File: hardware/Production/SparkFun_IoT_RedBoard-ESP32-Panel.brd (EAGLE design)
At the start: 172.2 x 137.9 mm, 850 parts, among them J1 5.5x2.1mm Barrel, J13 QWIIC_RIGHT_ANGLE, J15 MICRO-SD-PUSH-PUSH-EXT-PIN, J2 USB C, J21 USB C, J22 USB_SOLDER_PADS, J23 M10NO_SILK, J28 QWIIC_RIGHT_ANGLE, J29 MICRO-SD-PUSH-PUSH-EXT-PIN, J3 USB_SOLDER_PADS, J30 5.5x2.1mm Barrel, J37 USB C, J38 USB_SOLDER_PADS, J39 M10NO_SILK, J44 QWIIC_RIGHT_ANGLE, J45 MICRO-SD-PUSH-PUSH-EXT-PIN, J46 5.5x2.1mm Barrel, J5 M10NO_SILK, J53 USB C, J54 USB_SOLDER_PADS, J55 M10NO_SILK, J60 QWIIC_RIGHT_ANGLE, J61 MICRO-SD-PUSH-PUSH-EXT-PIN, J62 5.5x2.1mm Barrel, Q1 MBT3904DW1T1, Q11 20V/4.2A/52mΩ/1.4W, Q13 20V/4.2A/52mΩ/1.4W, Q14 MBT3904DW1T1, Q16 20V/4.2A/52mΩ/1.4W, Q18 20V/4.2A/52mΩ/1.4W, Q20 20V/4.2A/52mΩ/1.4W, Q22 20V/4.2A/52mΩ/1.4W, Q24 20V/4.2A/52mΩ/1.4W, Q26 20V/4.2A/52mΩ/1.4W, Q27 MBT3904DW1T1, Q29 20V/4.2A/52mΩ/1.4W, Q3 20V/4.2A/52mΩ/1.4W, Q31 20V/4.2A/52mΩ/1.4W, Q33 20V/4.2A/52mΩ/1.4W, Q35 20V/4.2A/52mΩ/1.4W, Q37 20V/4.2A/52mΩ/1.4W, Q39 20V/4.2A/52mΩ/1.4W, Q40 MBT3904DW1T1, Q42 20V/4.2A/52mΩ/1.4W, Q44 20V/4.2A/52mΩ/1.4W, Q46 20V/4.2A/52mΩ/1.4W, Q48 20V/4.2A/52mΩ/1.4W, Q5 20V/4.2A/52mΩ/1.4W, Q50 20V/4.2A/52mΩ/1.4W, Q52 20V/4.2A/52mΩ/1.4W, Q7 20V/4.2A/52mΩ/1.4W, Q9 20V/4.2A/52mΩ/1.4W, U1 ESP-WROOM-3232D-NARROW, U10 3.3V, U11 MCP73831, U12 MAX17048, U13 CH340C, U14 ESP-WROOM-3232D-NARROW, U15 LM1117, U16 3.3V, U17 MCP73831, U18 MAX17048, U19 CH340C, U2 CH340C, U20 ESP-WROOM-3232D-NARROW, U21 LM1117, U22 3.3V, U23 MCP73831, U24 MAX17048, U3 LM1117, U4 3.3V, U5 MCP73831, U6 MAX17048, U7 CH340C, U8 ESP-WROOM-3232D-NARROW, U9 LM1117

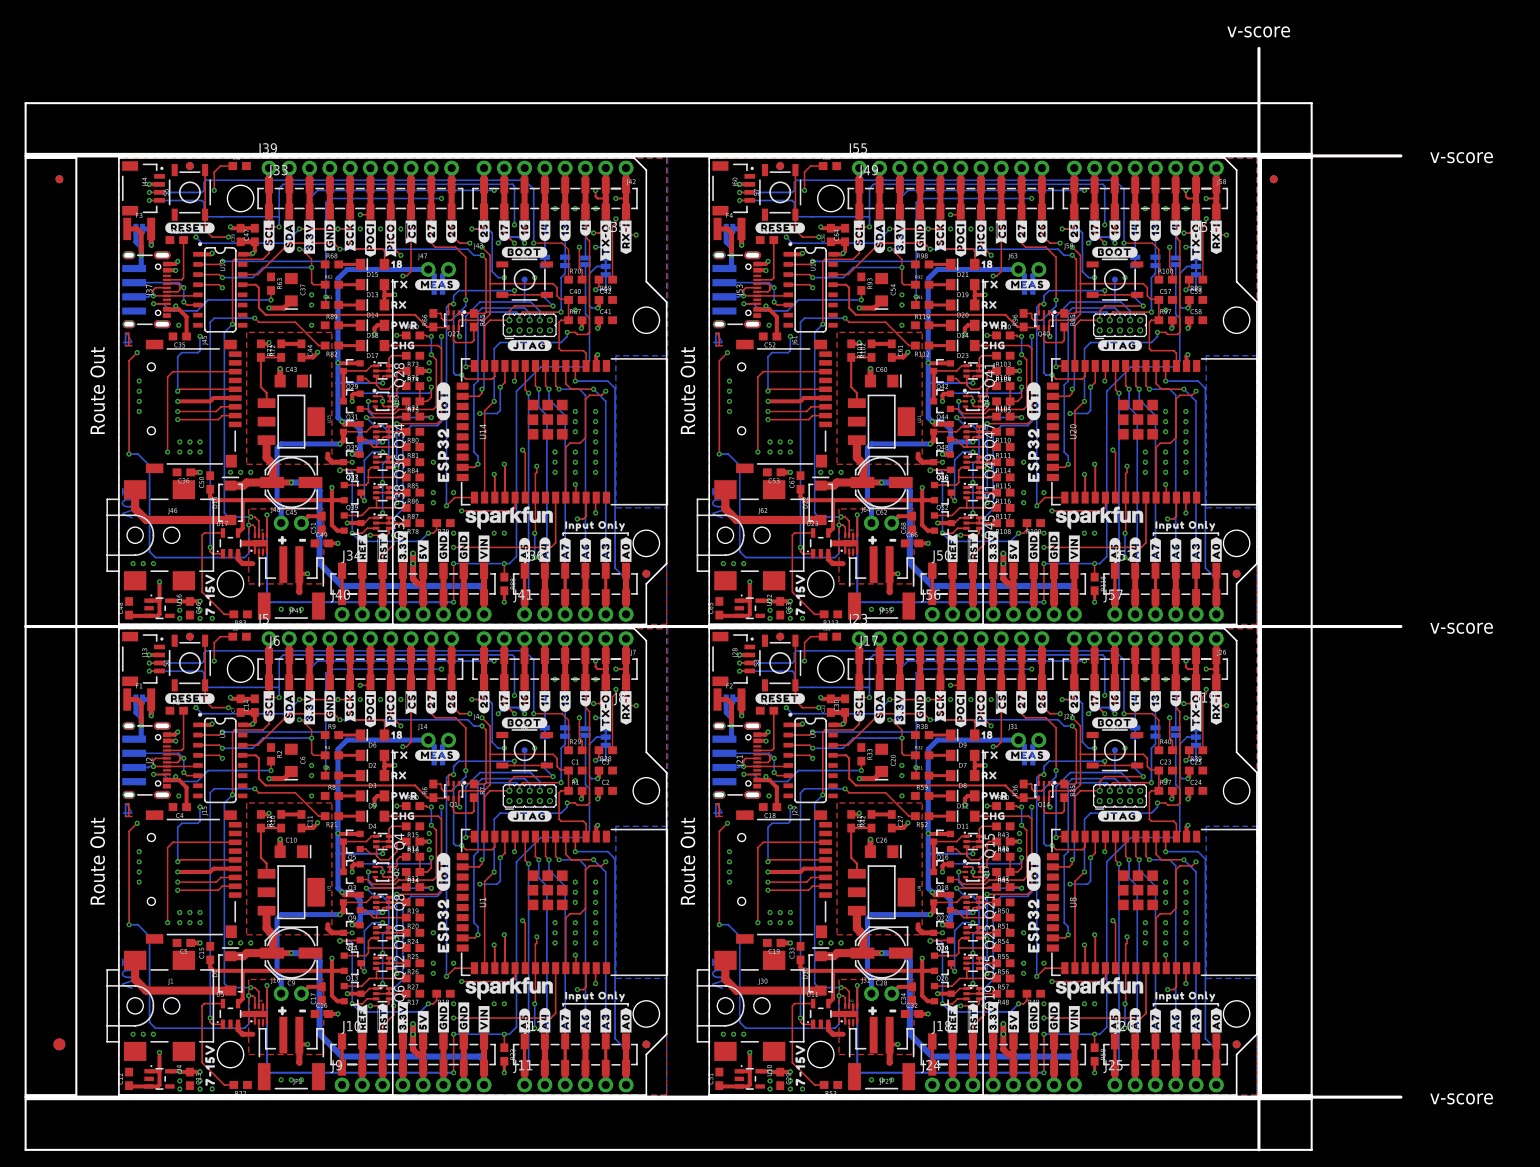
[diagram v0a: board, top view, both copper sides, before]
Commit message: Add production files for v02
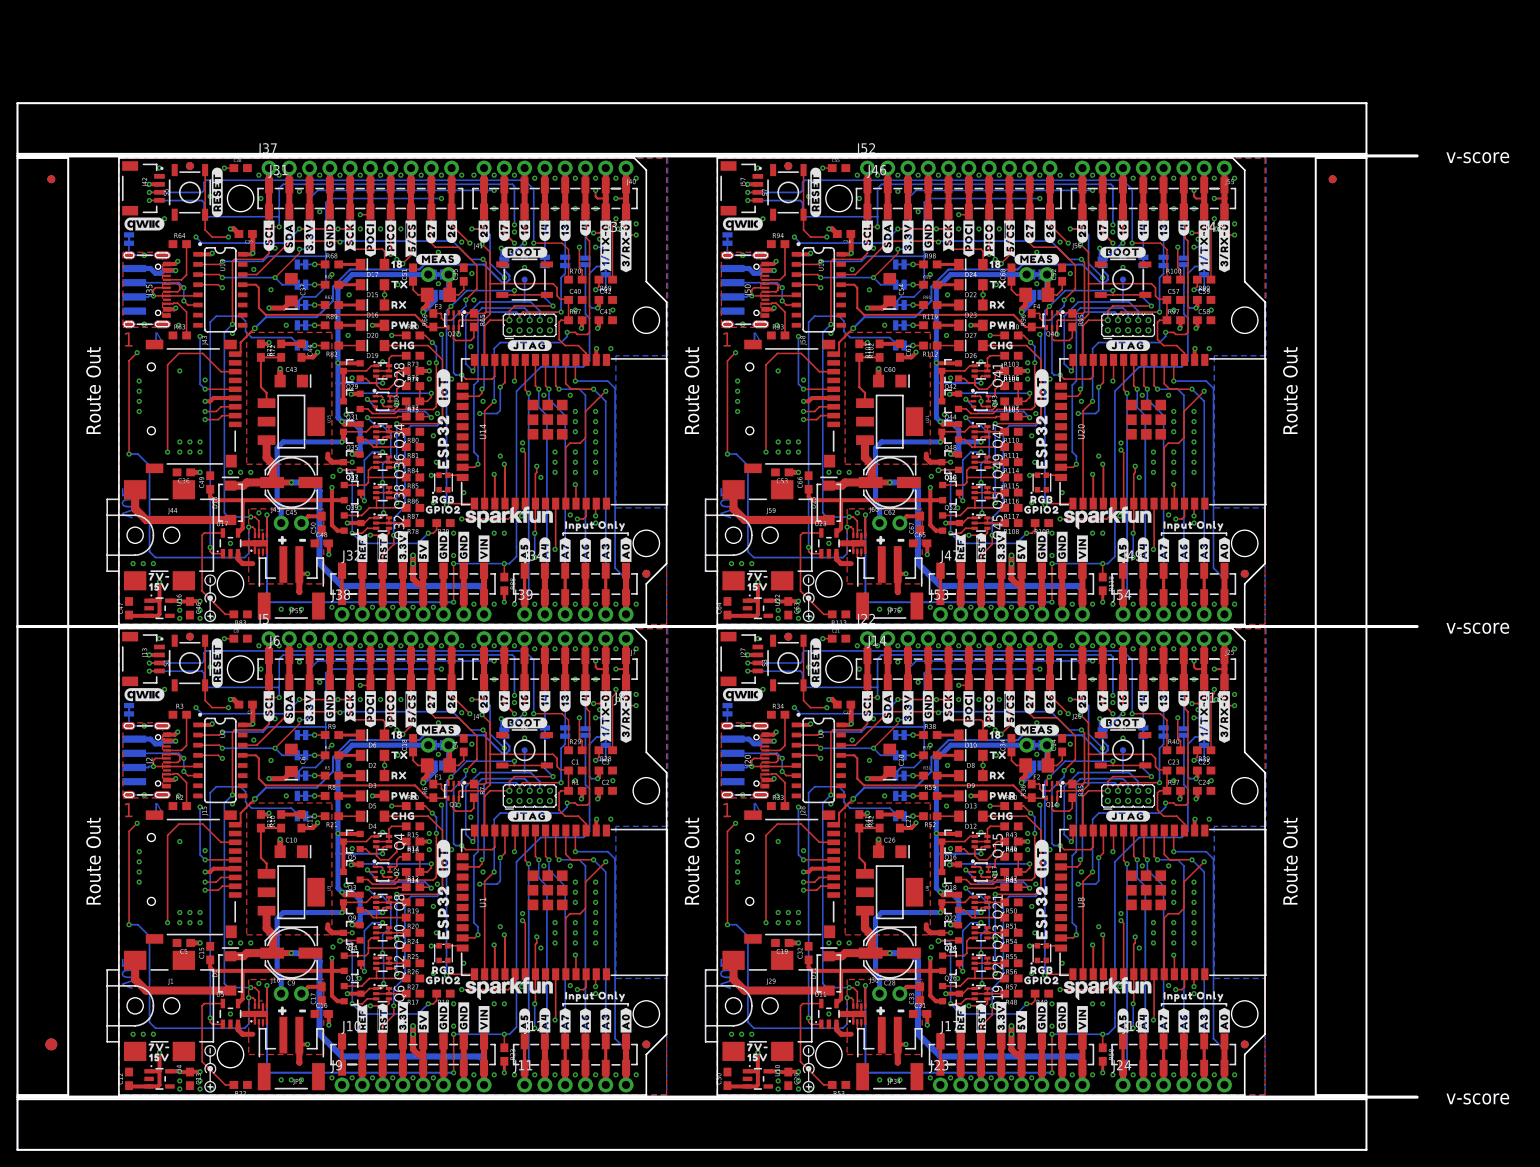
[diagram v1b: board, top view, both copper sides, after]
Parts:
- removed J61: MICRO-SD-PUSH-PUSH-EXT-PIN, SparkFun-Connectors:MICROSD-EXTERNALPIN
- removed J62: 5.5x2.1mm Barrel, SparkFun-Connectors:POWER_JACK_SMD
- removed J63, J64: (no value), SparkFun-Connectors:1X02_NO_SILK
- added D25: 3A/40V/500mV, SparkFun-DiscreteSemi:SMA-DIODE
- added D26: YELLOW, SparkFun-LED:LED-1206-HIDDENSILK
- added D27: GREEN, SparkFun-LED:LED-1206-HIDDENSILK
- added D28: WS2812_2020, SparkFun-LED:WS2812-2020
- added JP57, JP78: SHLD, SparkFun-Jumpers:SMT-JUMPER_2_NC_TRACE_SILK
- added JP58, JP79: SD_DET, SparkFun-Jumpers:SMT-JUMPER_2_NO_SILK
- added JP59, JP60, JP61, JP62, JP63, JP74, JP75, JP80, JP81, JP82, JP83, JP84: JUMPER-SMT_2_NC_TRACE_SILK, SparkFun-Jumpers:SMT-JUMPER_2_NC_TRACE_SILK
- added JP64, JP65, JP66, JP67: STAND-OFF, SparkFun-Hardware:STAND-OFF
- added JP68, JP69, JP70, JP71: FIDUCIAL1X2, SparkFun-Aesthetics:FIDUCIAL-1X2
- added JP72: JUMPER-SMT_3_2-NC_TRACE_SILK, SparkFun-Jumpers:SMT-JUMPER_3_2-NC_TRACE_SILK
- added JP73: JUMPER-SMT_2_NO_SILK, SparkFun-Jumpers:SMT-JUMPER_2_NO_SILK
- added JP76: LiPo, SparkFun-Connectors:JST-2-SMD
- added JP77: JUMPER-COMBO_2_NC_TRACE, SparkFun-Jumpers:COMBO-JUMPER_2_NC_TRACE
- added U$401: (no value), output-ESP32:G32321864
- added U$402: (no value), output-ESP32:#1849
- added U$403: (no value), output-ESP32:#1850
- added U$404: (no value), output-ESP32:#I2C#1855
- added U$405: (no value), output-ESP32:##ALERT##1852
- added U$406: (no value), output-ESP32:#TMS#1854
- added U$407: (no value), output-ESP32:#TCK#1853
- added U$408, U$409: (no value), output-ESP32:INPUT_ONLY321867
- added U$410: (no value), SparkFun-Aesthetics:REDBOARD_LOGO
- added U$411: (no value), output-ESP32:#IOT#132321869
- added U$412: (no value), output-ESP32:ESP32321856
- added U$413: (no value), output-ESP32:#IOT#132321874
- added U$414: (no value), output-ESP32:7#15V32321861
- added U$415: (no value), output-ESP32:3#3V_LOGIC_SHIELDS_ONLY132321876
- added U$416: (no value), output:#3#RX#0#0
- added U$417: (no value), output:#1#TX#0#0
- added U$418: (no value), output:#4##ALERT##0
- added U$419: (no value), output:#3#RX#0#4
- added U$420: (no value), output:#1#TX#0#2
- added U$421: (no value), output:#5##CS##0
- added U$422: (no value), output:#BYP#0
- added U$423: (no value), output:#SHLD#0
- added U$424: (no value), output:RGB0
- added U$425: (no value), output-ESP32:#MEAS#1851
- added U$426, U$427: (no value), SparkFun-Aesthetics:POLARITY_MARKING_CENTER_POSITIVE#JPG
- added U$428: (no value), output:7V#0
- added U$429: (no value), output:15V0
- added U$430: (no value), output:#SD_DET#0
- added U$431: (no value), output:#LED_18#0
- added U$432: (no value), output:#LED_TX#0
- added U$433: (no value), output:#LED_RX#0
- added U$434: (no value), output:#LED_PWR#0
- added U$435: (no value), output:#LED_CHG#0
- added U$436: (no value), output:GPIO20
- C14, C30, C47, C64: value 10uF -> 0.1uF
- C31, C48, C65: value 0.1uF -> 4.7uF
- C33, C50, C67: value 4.7uF -> 0.1uF
- D1: value 1A/40V/500mV -> 3A/40V/500mV
- D10: value 1A/40V/500mV -> BLUE; device SparkFun-DiscreteSemi:SMA-DIODE -> SparkFun-LED:LED-1206-HIDDENSILK
- D11: value RED -> 3A/40V/500mV; device SparkFun-LED:LED-1206-HIDDENSILK -> SparkFun-DiscreteSemi:SMA-DIODE
- D12: value PWR -> YELLOW
- D14: value YELLOW -> WS2812_2020; device SparkFun-LED:LED-1206-HIDDENSILK -> SparkFun-LED:WS2812-2020
- D15: value BLUE -> GREEN
- D16: value 1A/40V/500mV -> YELLOW; device SparkFun-DiscreteSemi:SMA-DIODE -> SparkFun-LED:LED-1206-HIDDENSILK
- D17: value RED -> BLUE
- D18: value PWR -> 3A/40V/500mV; device SparkFun-LED:LED-1206-HIDDENSILK -> SparkFun-DiscreteSemi:SMA-DIODE
- D19: value GREEN -> YELLOW
- D20, D8: value YELLOW -> GREEN
- D21: value BLUE -> WS2812_2020; device SparkFun-LED:LED-1206-HIDDENSILK -> SparkFun-LED:WS2812-2020
- D22: value 1A/40V/500mV -> GREEN; device SparkFun-DiscreteSemi:SMA-DIODE -> SparkFun-LED:LED-1206-HIDDENSILK
- D23, D4: value RED -> YELLOW
- D24: value PWR -> BLUE
- D5: value PWR -> GREEN
- D7: value GREEN -> WS2812_2020; device SparkFun-LED:LED-1206-HIDDENSILK -> SparkFun-LED:WS2812-2020
- D9: value BLUE -> YELLOW
- F1, F2, F3, F4: value 6V/2A -> 6V/0.75A/1.5A; device SparkFun-Fuses:1210 -> SparkFun-Fuses:1206
- J14, J31: device SparkFun-Connectors:1X02_NO_SILK -> SparkFun-Connectors:1X10_SMD_COMBINED
- J17, J33: device SparkFun-Connectors:1X10_SMD_COMBINED -> SparkFun-Connectors:1X08_SMD_COMBINED
- J19, J34: device SparkFun-Connectors:1X08_SMD_COMBINED -> SparkFun-Connectors:1X06_SMD_STRAIGHT_COMBO
- J2: value USB C -> USB-C; device SparkFun-Connectors:USB-C-16P-2LAYER-PADS -> SparkFun-Connectors:USB-C-16P-4LAYER-ISOLATED
- J20: value (none) -> USB-C; device SparkFun-Connectors:1X06_SMD_STRAIGHT_COMBO -> SparkFun-Connectors:USB-C-16P-4LAYER-ISOLATED
- J21: value USB C -> USB_SOLDER_PADS; device SparkFun-Connectors:USB-C-16P-2LAYER-PADS -> SparkFun-Connectors:USB-SOLDER-PADS
- J22: value USB_SOLDER_PADS -> M10NO_SILK; device SparkFun-Connectors:USB-SOLDER-PADS -> SparkFun-Connectors:1X10_NO_SILK
- J23, J55: value M10NO_SILK -> (none); device SparkFun-Connectors:1X10_NO_SILK -> SparkFun-Connectors:1X08_NO_SILK
- J24: device SparkFun-Connectors:1X08_NO_SILK -> SparkFun-Connectors:1X06_NO_SILK
- J25: device SparkFun-Connectors:1X06_NO_SILK -> SparkFun-Connectors:1X08_NO_SILK
- J26, J56: device SparkFun-Connectors:1X08_NO_SILK -> SparkFun-Connectors:2X5_PTH_SILK_.05
- J27: value (none) -> QWIIC_RIGHT_ANGLE; device SparkFun-Connectors:2X5_PTH_SILK_.05 -> SparkFun-Connectors:JST04_1MM_RA
- J28: value QWIIC_RIGHT_ANGLE -> MICRO-SD-PUSH-PUSH-EXT-PIN; device SparkFun-Connectors:JST04_1MM_RA -> SparkFun-Connectors:MICROSD-EXTERNALPIN
- J29: value MICRO-SD-PUSH-PUSH-EXT-PIN -> 5.5x2.1mm Barrel; device SparkFun-Connectors:MICROSD-EXTERNALPIN -> SparkFun-Connectors:POWER_JACK_SMD
- J30: value 5.5x2.1mm Barrel -> (none); device SparkFun-Connectors:POWER_JACK_SMD -> SparkFun-Connectors:1X02_NO_SILK
- J32, J47, J48: device SparkFun-Connectors:1X02_NO_SILK -> SparkFun-Connectors:1X08_SMD_COMBINED
- J35, J50: value (none) -> USB-C; device SparkFun-Connectors:1X08_SMD_COMBINED -> SparkFun-Connectors:USB-C-16P-4LAYER-ISOLATED
- J36: value (none) -> USB_SOLDER_PADS; device SparkFun-Connectors:1X06_SMD_STRAIGHT_COMBO -> SparkFun-Connectors:USB-SOLDER-PADS
- J37: value USB C -> M10NO_SILK; device SparkFun-Connectors:USB-C-16P-2LAYER-PADS -> SparkFun-Connectors:1X10_NO_SILK
- J38: value USB_SOLDER_PADS -> (none); device SparkFun-Connectors:USB-SOLDER-PADS -> SparkFun-Connectors:1X08_NO_SILK
- J39: value M10NO_SILK -> (none); device SparkFun-Connectors:1X10_NO_SILK -> SparkFun-Connectors:1X06_NO_SILK
- J41: device SparkFun-Connectors:1X06_NO_SILK -> SparkFun-Connectors:2X5_PTH_SILK_.05
- J42: value (none) -> QWIIC_RIGHT_ANGLE; device SparkFun-Connectors:1X08_NO_SILK -> SparkFun-Connectors:JST04_1MM_RA
- J43: value (none) -> MICRO-SD-PUSH-PUSH-EXT-PIN; device SparkFun-Connectors:2X5_PTH_SILK_.05 -> SparkFun-Connectors:MICROSD-EXTERNALPIN
- J44: value QWIIC_RIGHT_ANGLE -> 5.5x2.1mm Barrel; device SparkFun-Connectors:JST04_1MM_RA -> SparkFun-Connectors:POWER_JACK_SMD
- J45: value MICRO-SD-PUSH-PUSH-EXT-PIN -> (none); device SparkFun-Connectors:MICROSD-EXTERNALPIN -> SparkFun-Connectors:1X02_NO_SILK
- J46: value 5.5x2.1mm Barrel -> (none); device SparkFun-Connectors:POWER_JACK_SMD -> SparkFun-Connectors:1X10_SMD_COMBINED
- J49: device SparkFun-Connectors:1X10_SMD_COMBINED -> SparkFun-Connectors:1X06_SMD_STRAIGHT_COMBO
- J51: value (none) -> USB_SOLDER_PADS; device SparkFun-Connectors:1X08_SMD_COMBINED -> SparkFun-Connectors:USB-SOLDER-PADS
- J52: value (none) -> M10NO_SILK; device SparkFun-Connectors:1X06_SMD_STRAIGHT_COMBO -> SparkFun-Connectors:1X10_NO_SILK
- J53: value USB C -> (none); device SparkFun-Connectors:USB-C-16P-2LAYER-PADS -> SparkFun-Connectors:1X08_NO_SILK
- J54: value USB_SOLDER_PADS -> (none); device SparkFun-Connectors:USB-SOLDER-PADS -> SparkFun-Connectors:1X06_NO_SILK
- J57: value (none) -> QWIIC_RIGHT_ANGLE; device SparkFun-Connectors:1X06_NO_SILK -> SparkFun-Connectors:JST04_1MM_RA
- J58: value (none) -> MICRO-SD-PUSH-PUSH-EXT-PIN; device SparkFun-Connectors:1X08_NO_SILK -> SparkFun-Connectors:MICROSD-EXTERNALPIN
- J59: value (none) -> 5.5x2.1mm Barrel; device SparkFun-Connectors:2X5_PTH_SILK_.05 -> SparkFun-Connectors:POWER_JACK_SMD
- J60: value QWIIC_RIGHT_ANGLE -> (none); device SparkFun-Connectors:JST04_1MM_RA -> SparkFun-Connectors:1X02_NO_SILK
- JP10, JP56: value JUMPER-SMT_2_NC_TRACE_SILK -> JUMPER-COMBO_2_NC_TRACE; device SparkFun-Jumpers:SMT-JUMPER_2_NC_TRACE_SILK -> SparkFun-Jumpers:COMBO-JUMPER_2_NC_TRACE
- JP15: value STAND-OFF -> SHLD; device SparkFun-Hardware:STAND-OFF -> SparkFun-Jumpers:SMT-JUMPER_2_NC_TRACE_SILK
- JP16: value STAND-OFF -> SD_DET; device SparkFun-Hardware:STAND-OFF -> SparkFun-Jumpers:SMT-JUMPER_2_NO_SILK
- JP17, JP18, JP32: value STAND-OFF -> JUMPER-SMT_2_NC_TRACE_SILK; device SparkFun-Hardware:STAND-OFF -> SparkFun-Jumpers:SMT-JUMPER_2_NC_TRACE_SILK
- JP19, JP20, JP21, JP33: value FIDUCIAL1X2 -> JUMPER-SMT_2_NC_TRACE_SILK; device SparkFun-Aesthetics:FIDUCIAL-1X2 -> SparkFun-Jumpers:SMT-JUMPER_2_NC_TRACE_SILK
- JP22: value FIDUCIAL1X2 -> STAND-OFF; device SparkFun-Aesthetics:FIDUCIAL-1X2 -> SparkFun-Hardware:STAND-OFF
- JP23: value JUMPER-SMT_3_2-NC_TRACE_SILK -> STAND-OFF; device SparkFun-Jumpers:SMT-JUMPER_3_2-NC_TRACE_SILK -> SparkFun-Hardware:STAND-OFF
- JP24: value JUMPER-SMT_2_NO_SILK -> STAND-OFF; device SparkFun-Jumpers:SMT-JUMPER_2_NO_SILK -> SparkFun-Hardware:STAND-OFF
- JP25: value JUMPER-SMT_2_NC_TRACE_SILK -> STAND-OFF; device SparkFun-Jumpers:SMT-JUMPER_2_NC_TRACE_SILK -> SparkFun-Hardware:STAND-OFF
- JP26, JP28: value JUMPER-SMT_2_NC_TRACE_SILK -> FIDUCIAL1X2; device SparkFun-Jumpers:SMT-JUMPER_2_NC_TRACE_SILK -> SparkFun-Aesthetics:FIDUCIAL-1X2
- JP27: value LiPo -> FIDUCIAL1X2; device SparkFun-Connectors:JST-2-SMD -> SparkFun-Aesthetics:FIDUCIAL-1X2
- JP29: value STAND-OFF -> FIDUCIAL1X2; device SparkFun-Hardware:STAND-OFF -> SparkFun-Aesthetics:FIDUCIAL-1X2
- JP30: value STAND-OFF -> JUMPER-SMT_3_2-NC_TRACE_SILK; device SparkFun-Hardware:STAND-OFF -> SparkFun-Jumpers:SMT-JUMPER_3_2-NC_TRACE_SILK
- JP31: value STAND-OFF -> JUMPER-SMT_2_NO_SILK; device SparkFun-Hardware:STAND-OFF -> SparkFun-Jumpers:SMT-JUMPER_2_NO_SILK
- JP34: value FIDUCIAL1X2 -> LiPo; device SparkFun-Aesthetics:FIDUCIAL-1X2 -> SparkFun-Connectors:JST-2-SMD
- JP35: value FIDUCIAL1X2 -> JUMPER-COMBO_2_NC_TRACE; device SparkFun-Aesthetics:FIDUCIAL-1X2 -> SparkFun-Jumpers:COMBO-JUMPER_2_NC_TRACE
- JP36: value FIDUCIAL1X2 -> SHLD; device SparkFun-Aesthetics:FIDUCIAL-1X2 -> SparkFun-Jumpers:SMT-JUMPER_2_NC_TRACE_SILK
- JP37: value JUMPER-SMT_3_2-NC_TRACE_SILK -> SD_DET; device SparkFun-Jumpers:SMT-JUMPER_3_2-NC_TRACE_SILK -> SparkFun-Jumpers:SMT-JUMPER_2_NO_SILK
- JP38: value JUMPER-SMT_2_NO_SILK -> JUMPER-SMT_2_NC_TRACE_SILK; device SparkFun-Jumpers:SMT-JUMPER_2_NO_SILK -> SparkFun-Jumpers:SMT-JUMPER_2_NC_TRACE_SILK
- JP41: value LiPo -> JUMPER-SMT_2_NC_TRACE_SILK; device SparkFun-Connectors:JST-2-SMD -> SparkFun-Jumpers:SMT-JUMPER_2_NC_TRACE_SILK
- R108, R110, R114, R116, R17, R19, R24, R26, R48, R50, R54, R56, R78, R80, R84, R86: value 10k -> 100k
- R109, R111, R115, R117, R18, R20, R25, R27, R49, R51, R55, R57, R79, R81, R85, R87: value 47k -> 1M
- R119, R59, R8, R89: value 10k -> 2.2k
- R31, R32, R4, R5, R61, R62, R91, R92: value 4.7k -> 1k
- U$102: device output-ESP32:#SDA#33 -> output:#4##ALERT##0
- U$104: device output-ESP32:#3#3V#33 -> output:#1#TX#0#0
- U$105: device output-ESP32:#GND#32 -> output:#1#TX#0#2
- U$106: device output-ESP32:#SCK#31 -> output:7V#0
- U$107: device output-ESP32:#POCI#30 -> output:15V0
- U$108: device output-ESP32:#PICO#29 -> output:#SD_DET#0
- U$109: device output-ESP32:1836 -> output:#LED_TX#0
- U$11: device output-ESP32:##CS##28 -> output-ESP32:#MEAS#1851
- U$110: device output-ESP32:##CS##28 -> output:#LED_RX#0
- U$111: device output-ESP32:#27#27 -> output:#LED_PWR#0
- U$112: device output-ESP32:#26#26 -> output:#LED_CHG#0
- U$113: device output-ESP32:TX1838 -> output:GPIO20
- U$114: device output-ESP32:RX1839 -> output-ESP32:#GND#32
- U$115: device output-ESP32:PWR1837 -> output-ESP32:#SCK#31
- U$116: device output-ESP32:CHG1840 -> output-ESP32:#POCI#30
- U$117: device output-ESP32:#25#18 -> output-ESP32:#PICO#29
- U$118: device output-ESP32:#17#17 -> output-ESP32:1836
- U$119: device output-ESP32:#16#15 -> output-ESP32:#27#27
- U$120: device output-ESP32:#14#14 -> output-ESP32:#26#26
- U$121: device output-ESP32:#13#5 -> output-ESP32:TX1838
- U$122: device output-ESP32:#4#2 -> output-ESP32:RX1839
- U$123: device output-ESP32:#TX#O#0 -> output-ESP32:PWR1837
- U$124: device output-ESP32:#RX#I#1 -> output-ESP32:CHG1840
- U$125: device output-ESP32:#RESET#1842 -> output-ESP32:#25#18
- U$126: device output-ESP32:#BOOT#1841 -> output-ESP32:#17#17
- U$127, U$345: device output-ESP32:#JTAG#1847 -> output-ESP32:#16#15
- U$128: device output-ESP32:#A0#1843 -> output-ESP32:#14#14
- U$129: device output-ESP32:#A3#1843 -> output-ESP32:#13#5
- U$130: device output-ESP32:#A6#1843 -> output-ESP32:#4#2
- U$131: device output-ESP32:#A7#1843 -> output-ESP32:#RESET#1842
- U$132: device output-ESP32:#A4#1843 -> output-ESP32:#BOOT#1841
- U$133: device output-ESP32:#A5#1843 -> output-ESP32:#JTAG#1847
- U$134: device output-ESP32:#VIN#1843 -> output-ESP32:#A0#1843
- U$135: device output-ESP32:#GND#1844 -> output-ESP32:#A3#1843
- U$136: device output-ESP32:#GND#1844 -> output-ESP32:#A6#1843
- U$137: device output-ESP32:#5V#1845 -> output-ESP32:#A7#1843
- U$138: device output-ESP32:#3#3V#1845 -> output-ESP32:#A4#1843
- U$139: device output-ESP32:##RST##1845 -> output-ESP32:#A5#1843
- U$140: device output-ESP32:#REF#1846 -> output-ESP32:#VIN#1843
- U$141: device output-ESP32:#MEAS#1851 -> output-ESP32:#GND#1844
- U$142: device output-ESP32:#1849 -> output-ESP32:#GND#1844
- U$143: device output-ESP32:#1850 -> output-ESP32:#5V#1845
- U$144: device output-ESP32:#BATT#1848 -> output-ESP32:#3#3V#1845
- U$145: device output-ESP32:#JTAG#1847 -> output-ESP32:##RST##1845
- U$146: device output-ESP32:ESP321855 -> output-ESP32:#REF#1846
- U$147: device output-ESP32:7#15V32321861 -> output-ESP32:#MEAS#1851
- U$148: device output-ESP32:#39#A3#321862 -> output-ESP32:#1849
- U$149: device output-ESP32:#36#A0#321862 -> output-ESP32:#1850
- U$150: device output-ESP32:#34#A6#32321865 -> output-ESP32:#BATT#1848
- U$151, U$351: device output-ESP32:#35#A7#321862 -> output-ESP32:#JTAG#1847
- U$152: device output-ESP32:#32#A4#32321865 -> output-ESP32:ESP321855
- U$153: device output-ESP32:#34#A6#321862 -> output-ESP32:#39#A3#321862
- U$154: device output-ESP32:#VIN#321862 -> output-ESP32:#36#A0#321862
- U$155: device output-ESP32:#GND#321863 -> output-ESP32:#34#A6#32321865
- U$156: device output-ESP32:#5V#321864 -> output-ESP32:#35#A7#321862
- U$157: device output-ESP32:#3#3V#321864 -> output-ESP32:#32#A4#32321865
- U$158: device output-ESP32:#GND#321863 -> output-ESP32:#34#A6#321862
- U$159: device output-ESP32:##RESET##321864 -> output-ESP32:#VIN#321862
- U$160: device output-ESP32:#IOREF#321865 -> output-ESP32:#GND#321863
- U$161: device output-ESP32:#3#RX#I#32321869 -> output-ESP32:#5V#321864
- U$162: device output-ESP32:#1#TX#O#32321869 -> output-ESP32:#3#3V#321864
- U$163: device output-ESP32:#13#TCK#32321869 -> output-ESP32:#GND#321863
- U$164: device output-ESP32:#14#TMS#32321869 -> output-ESP32:##RESET##321864
- U$165: device output-ESP32:#16#32321869 -> output-ESP32:#IOREF#321865
- U$166: device output-ESP32:#17#32321869 -> output-ESP32:#13#TCK#32321869
- U$167: device output-ESP32:#25#32321869 -> output-ESP32:#14#TMS#32321869
- U$168: device output-ESP32:#26#32321869 -> output-ESP32:#16#32321869
- U$169: device output-ESP32:#5##CS##32321869 -> output-ESP32:#17#32321869
- U$170: device output-ESP32:#23#PICO#321866 -> output-ESP32:#25#32321869
- U$171: device output-ESP32:#19#POCI#321866 -> output-ESP32:#26#32321869
- U$172: device output-ESP32:#18#SCK#32321869 -> output-ESP32:#5##CS##32321869
- U$173: device output-ESP32:#21#SDA#32321869 -> output-ESP32:#23#PICO#321866
- U$174: device output-ESP32:#22#SCL#32321869 -> output-ESP32:#19#POCI#321866
- U$175: device output-ESP32:#27#32321869 -> output-ESP32:#18#SCK#32321869
- U$176: device output-ESP32:#GND#321866 -> output-ESP32:#21#SDA#32321869
- U$177: device output-ESP32:#3#3V#321866 -> output-ESP32:#22#SCL#32321869
- U$178: device output-ESP32:#MEAS#1851 -> output-ESP32:#27#32321869
- U$179: device output-ESP32:#BYP#35 -> output-ESP32:#GND#321866
- U$180: device output-ESP32:D#32321863 -> output-ESP32:#3#3V#321866
- U$181: device output-ESP32:D#32321862 -> output-ESP32:D#32321863
- U$182: device output-ESP32:G32321864 -> output-ESP32:D#32321862
- U$183: device output-ESP32:#1849 -> output-ESP32:G32321864
- U$184: device output-ESP32:#1850 -> output-ESP32:#1849
- U$185: device output-ESP32:#I2C#1855 -> output-ESP32:#1850
- U$186: device output-ESP32:##ALERT##1852 -> output-ESP32:#I2C#1855
- U$187: device output-ESP32:#TMS#1854 -> output-ESP32:##ALERT##1852
- U$188: device output-ESP32:#TCK#1853 -> output-ESP32:#TMS#1854
- U$189: device output-ESP32:INPUT_ONLY321867 -> output-ESP32:#TCK#1853
- U$191: device output-ESP32:##ALERT##4#321866 -> output-ESP32:INPUT_ONLY321867
- U$192: device output-ESP32:TP1321868 -> SparkFun-Aesthetics:REDBOARD_LOGO
- U$193: device SparkFun-Aesthetics:REDBOARD_LOGO -> output-ESP32:#IOT#132321869
- U$194: device output-ESP32:#IOT#132321869 -> output-ESP32:ESP32321856
- U$195: device output-ESP32:ESP32321856 -> output-ESP32:#IOT#132321874
- U$196: device output-ESP32:#IOT#132321874 -> output-ESP32:7#15V32321861
- U$197: device output-ESP32:MADE_IN32321857 -> output-ESP32:3#3V_LOGIC_SHIELDS_ONLY132321876
- U$198: device output-ESP32:THE_USA32321858 -> output:#3#RX#0#0
- U$199: device output-ESP32:7#15V32321861 -> output:#1#TX#0#0
- U$200: device output-ESP32:3#3V_LOGIC_SHIELDS_ONLY132321876 -> output:#4##ALERT##0
- U$201: device output-ESP32:V323252 -> output:#3#RX#0#4
- U$202: device output-ESP32:#SCL#34 -> output:#1#TX#0#2
- U$203: device output-ESP32:#SDA#33 -> output:#5##CS##0
- U$204: device output-ESP32:#3#3V#33 -> output:#BYP#0
- U$205: device output-ESP32:#GND#32 -> output:#SHLD#0
- U$206: device output-ESP32:#SCK#31 -> output:RGB0
- U$207: device output-ESP32:#POCI#30 -> output-ESP32:#MEAS#1851
- U$208: device output-ESP32:#PICO#29 -> SparkFun-Aesthetics:POLARITY_MARKING_CENTER_POSITIVE#JPG
- U$209: device output-ESP32:1836 -> SparkFun-Aesthetics:POLARITY_MARKING_CENTER_POSITIVE#JPG
- U$210: device output-ESP32:##CS##28 -> output:7V#0
- U$211: device output-ESP32:#27#27 -> output:15V0
- U$212: device output-ESP32:#26#26 -> output:#SD_DET#0
- U$213: device output-ESP32:TX1838 -> output:#LED_18#0
- U$214: device output-ESP32:RX1839 -> output:#LED_TX#0
- U$215: device output-ESP32:PWR1837 -> output:#LED_RX#0
- U$216: device output-ESP32:CHG1840 -> output:#LED_PWR#0
- U$217: device output-ESP32:#25#18 -> output:#LED_CHG#0
- U$218: device output-ESP32:#17#17 -> output:GPIO20
- U$219: device output-ESP32:#16#15 -> output-ESP32:V323252
- U$220: device output-ESP32:#14#14 -> output-ESP32:#SCL#34
- U$221: device output-ESP32:#13#5 -> output-ESP32:#SDA#33
- U$222: device output-ESP32:#4#2 -> output-ESP32:#3#3V#33
- U$223: device output-ESP32:#TX#O#0 -> output-ESP32:#GND#32
- U$224: device output-ESP32:#RX#I#1 -> output-ESP32:#SCK#31
- U$225: device output-ESP32:#RESET#1842 -> output-ESP32:#POCI#30
- U$226: device output-ESP32:#BOOT#1841 -> output-ESP32:#PICO#29
- U$227: device output-ESP32:#JTAG#1847 -> output-ESP32:1836
- U$228: device output-ESP32:#A0#1843 -> output-ESP32:#27#27
- U$229: device output-ESP32:#A3#1843 -> output-ESP32:#26#26
- U$230: device output-ESP32:#A6#1843 -> output-ESP32:TX1838
- U$231: device output-ESP32:#A7#1843 -> output-ESP32:RX1839
- U$232: device output-ESP32:#A4#1843 -> output-ESP32:PWR1837
- U$233: device output-ESP32:#A5#1843 -> output-ESP32:CHG1840
- U$234: device output-ESP32:#VIN#1843 -> output-ESP32:#25#18
- U$235: device output-ESP32:#GND#1844 -> output-ESP32:#17#17
- U$236: device output-ESP32:#GND#1844 -> output-ESP32:#16#15
- U$237: device output-ESP32:#5V#1845 -> output-ESP32:#14#14
- U$238: device output-ESP32:#3#3V#1845 -> output-ESP32:#13#5
- U$239: device output-ESP32:##RST##1845 -> output-ESP32:#4#2
- U$24: device output-ESP32:#TX#O#0 -> output:#3#RX#0#4
- U$240: device output-ESP32:#REF#1846 -> output-ESP32:#RESET#1842
- U$241: device output-ESP32:#MEAS#1851 -> output-ESP32:#BOOT#1841
- U$242: device output-ESP32:#1849 -> output-ESP32:#JTAG#1847
- U$243: device output-ESP32:#1850 -> output-ESP32:#A0#1843
- U$244: device output-ESP32:#BATT#1848 -> output-ESP32:#A3#1843
- U$245: device output-ESP32:#JTAG#1847 -> output-ESP32:#A6#1843
- U$246: device output-ESP32:ESP321855 -> output-ESP32:#A7#1843
- U$247: device output-ESP32:7#15V32321861 -> output-ESP32:#A4#1843
- U$248: device output-ESP32:#39#A3#321862 -> output-ESP32:#A5#1843
- U$249: device output-ESP32:#36#A0#321862 -> output-ESP32:#VIN#1843
- U$25: device output-ESP32:#RX#I#1 -> output:#3#RX#0#0
- U$250: device output-ESP32:#34#A6#32321865 -> output-ESP32:#GND#1844
- U$251: device output-ESP32:#35#A7#321862 -> output-ESP32:#GND#1844
- U$252: device output-ESP32:#32#A4#32321865 -> output-ESP32:#5V#1845
- U$253: device output-ESP32:#34#A6#321862 -> output-ESP32:#3#3V#1845
- U$254: device output-ESP32:#VIN#321862 -> output-ESP32:##RST##1845
- U$255: device output-ESP32:#GND#321863 -> output-ESP32:#REF#1846
- U$256: device output-ESP32:#5V#321864 -> output-ESP32:#MEAS#1851
- U$257: device output-ESP32:#3#3V#321864 -> output-ESP32:#1849
- U$258: device output-ESP32:#GND#321863 -> output-ESP32:#1850
- U$259: device output-ESP32:##RESET##321864 -> output-ESP32:#BATT#1848
- U$260: device output-ESP32:#IOREF#321865 -> output-ESP32:#JTAG#1847
- U$261: device output-ESP32:#3#RX#I#32321869 -> output-ESP32:ESP321855
- U$262: device output-ESP32:#1#TX#O#32321869 -> output-ESP32:#39#A3#321862
- U$263: device output-ESP32:#13#TCK#32321869 -> output-ESP32:#36#A0#321862
- U$264: device output-ESP32:#14#TMS#32321869 -> output-ESP32:#34#A6#32321865
- U$265: device output-ESP32:#16#32321869 -> output-ESP32:#35#A7#321862
- U$266: device output-ESP32:#17#32321869 -> output-ESP32:#32#A4#32321865
- U$267: device output-ESP32:#25#32321869 -> output-ESP32:#34#A6#321862
- U$268: device output-ESP32:#26#32321869 -> output-ESP32:#VIN#321862
- U$269: device output-ESP32:#5##CS##32321869 -> output-ESP32:#GND#321863
- U$270: device output-ESP32:#23#PICO#321866 -> output-ESP32:#5V#321864
- U$271: device output-ESP32:#19#POCI#321866 -> output-ESP32:#3#3V#321864
- U$272: device output-ESP32:#18#SCK#32321869 -> output-ESP32:#GND#321863
- U$273: device output-ESP32:#21#SDA#32321869 -> output-ESP32:##RESET##321864
- U$274: device output-ESP32:#22#SCL#32321869 -> output-ESP32:#IOREF#321865
- U$275: device output-ESP32:#27#32321869 -> output-ESP32:#13#TCK#32321869
- U$276: device output-ESP32:#GND#321866 -> output-ESP32:#14#TMS#32321869
- U$277: device output-ESP32:#3#3V#321866 -> output-ESP32:#16#32321869
- U$278: device output-ESP32:#MEAS#1851 -> output-ESP32:#17#32321869
- U$279: device output-ESP32:#BYP#35 -> output-ESP32:#25#32321869
- U$280: device output-ESP32:D#32321863 -> output-ESP32:#26#32321869
- U$281: device output-ESP32:D#32321862 -> output-ESP32:#5##CS##32321869
- U$282: device output-ESP32:G32321864 -> output-ESP32:#23#PICO#321866
- U$283: device output-ESP32:#1849 -> output-ESP32:#19#POCI#321866
- U$284: device output-ESP32:#1850 -> output-ESP32:#18#SCK#32321869
- U$285: device output-ESP32:#I2C#1855 -> output-ESP32:#21#SDA#32321869
- U$286: device output-ESP32:##ALERT##1852 -> output-ESP32:#22#SCL#32321869
- U$287: device output-ESP32:#TMS#1854 -> output-ESP32:#27#32321869
- U$288: device output-ESP32:#TCK#1853 -> output-ESP32:#GND#321866
- U$289: device output-ESP32:INPUT_ONLY321867 -> output-ESP32:#3#3V#321866
- U$290: device output-ESP32:INPUT_ONLY321867 -> output-ESP32:D#32321863
- U$291: device output-ESP32:##ALERT##4#321866 -> output-ESP32:D#32321862
- U$292: device output-ESP32:TP1321868 -> output-ESP32:G32321864
- U$293: device SparkFun-Aesthetics:REDBOARD_LOGO -> output-ESP32:#1849
- U$294: device output-ESP32:#IOT#132321869 -> output-ESP32:#1850
- U$295: device output-ESP32:ESP32321856 -> output-ESP32:#I2C#1855
- U$296: device output-ESP32:#IOT#132321874 -> output-ESP32:##ALERT##1852
- U$297: device output-ESP32:MADE_IN32321857 -> output-ESP32:#TMS#1854
- U$298: device output-ESP32:THE_USA32321858 -> output-ESP32:#TCK#1853
- U$299: device output-ESP32:7#15V32321861 -> output-ESP32:INPUT_ONLY321867
- U$300: device output-ESP32:3#3V_LOGIC_SHIELDS_ONLY132321876 -> output-ESP32:INPUT_ONLY321867
- U$301: device output-ESP32:V323252 -> SparkFun-Aesthetics:REDBOARD_LOGO
- U$302: device output-ESP32:#SCL#34 -> output-ESP32:#IOT#132321869
- U$303: device output-ESP32:#SDA#33 -> output-ESP32:ESP32321856
- U$304: device output-ESP32:#3#3V#33 -> output-ESP32:#IOT#132321874
- U$305: device output-ESP32:#GND#32 -> output-ESP32:7#15V32321861
- U$306: device output-ESP32:#SCK#31 -> output-ESP32:3#3V_LOGIC_SHIELDS_ONLY132321876
- U$307: device output-ESP32:#POCI#30 -> output:#3#RX#0#0
- U$308: device output-ESP32:#PICO#29 -> output:#1#TX#0#0
- U$309: device output-ESP32:1836 -> output:#4##ALERT##0
- U$310: device output-ESP32:##CS##28 -> output:#3#RX#0#4
- U$311: device output-ESP32:#27#27 -> output:#1#TX#0#2
- U$312: device output-ESP32:#26#26 -> output:#5##CS##0
- U$313: device output-ESP32:TX1838 -> output:#BYP#0
- U$314: device output-ESP32:RX1839 -> output:#SHLD#0
- U$315: device output-ESP32:PWR1837 -> output:RGB0
- U$316: device output-ESP32:CHG1840 -> output-ESP32:#MEAS#1851
- U$317: device output-ESP32:#25#18 -> SparkFun-Aesthetics:POLARITY_MARKING_CENTER_POSITIVE#JPG
- U$318: device output-ESP32:#17#17 -> SparkFun-Aesthetics:POLARITY_MARKING_CENTER_POSITIVE#JPG
- U$319: device output-ESP32:#16#15 -> output:7V#0
- U$320: device output-ESP32:#14#14 -> output:15V0
- U$321: device output-ESP32:#13#5 -> output:#SD_DET#0
- U$322: device output-ESP32:#4#2 -> output:#LED_18#0
- U$323: device output-ESP32:#TX#O#0 -> output:#LED_TX#0
- U$324: device output-ESP32:#RX#I#1 -> output:#LED_RX#0
- U$325: device output-ESP32:#RESET#1842 -> output:#LED_PWR#0
- U$326: device output-ESP32:#BOOT#1841 -> output:#LED_CHG#0
- U$327: device output-ESP32:#JTAG#1847 -> output:GPIO20
- U$328: device output-ESP32:#A0#1843 -> output-ESP32:V323252
- U$329: device output-ESP32:#A3#1843 -> output-ESP32:#SCL#34
- U$330: device output-ESP32:#A6#1843 -> output-ESP32:#SDA#33
- U$331: device output-ESP32:#A7#1843 -> output-ESP32:#3#3V#33
- U$332: device output-ESP32:#A4#1843 -> output-ESP32:#GND#32
- U$333: device output-ESP32:#A5#1843 -> output-ESP32:#SCK#31
- U$334: device output-ESP32:#VIN#1843 -> output-ESP32:#POCI#30
- U$335: device output-ESP32:#GND#1844 -> output-ESP32:#PICO#29
- U$336: device output-ESP32:#GND#1844 -> output-ESP32:1836
- U$337: device output-ESP32:#5V#1845 -> output-ESP32:#27#27
- U$338: device output-ESP32:#3#3V#1845 -> output-ESP32:#26#26
- U$339: device output-ESP32:##RST##1845 -> output-ESP32:TX1838
- U$340: device output-ESP32:#REF#1846 -> output-ESP32:RX1839
- U$341: device output-ESP32:#MEAS#1851 -> output-ESP32:PWR1837
- U$342: device output-ESP32:#1849 -> output-ESP32:CHG1840
- U$343: device output-ESP32:#1850 -> output-ESP32:#25#18
- U$344: device output-ESP32:#BATT#1848 -> output-ESP32:#17#17
- U$346: device output-ESP32:ESP321855 -> output-ESP32:#14#14
- U$347: device output-ESP32:7#15V32321861 -> output-ESP32:#13#5
- U$348: device output-ESP32:#39#A3#321862 -> output-ESP32:#4#2
- U$349: device output-ESP32:#36#A0#321862 -> output-ESP32:#RESET#1842
- U$350: device output-ESP32:#34#A6#32321865 -> output-ESP32:#BOOT#1841
- U$352: device output-ESP32:#32#A4#32321865 -> output-ESP32:#A0#1843
- U$353: device output-ESP32:#34#A6#321862 -> output-ESP32:#A3#1843
- U$354: device output-ESP32:#VIN#321862 -> output-ESP32:#A6#1843
- U$355: device output-ESP32:#GND#321863 -> output-ESP32:#A7#1843
- U$356: device output-ESP32:#5V#321864 -> output-ESP32:#A4#1843
- U$357: device output-ESP32:#3#3V#321864 -> output-ESP32:#A5#1843
- U$358: device output-ESP32:#GND#321863 -> output-ESP32:#VIN#1843
- U$359: device output-ESP32:##RESET##321864 -> output-ESP32:#GND#1844
- U$360: device output-ESP32:#IOREF#321865 -> output-ESP32:#GND#1844
- U$361: device output-ESP32:#3#RX#I#32321869 -> output-ESP32:#5V#1845
- U$362: device output-ESP32:#1#TX#O#32321869 -> output-ESP32:#3#3V#1845
- U$363: device output-ESP32:#13#TCK#32321869 -> output-ESP32:##RST##1845
- U$364: device output-ESP32:#14#TMS#32321869 -> output-ESP32:#REF#1846
- U$365: device output-ESP32:#16#32321869 -> output-ESP32:#MEAS#1851
- U$366: device output-ESP32:#17#32321869 -> output-ESP32:#1849
- U$367: device output-ESP32:#25#32321869 -> output-ESP32:#1850
- U$368: device output-ESP32:#26#32321869 -> output-ESP32:#BATT#1848
- U$369: device output-ESP32:#5##CS##32321869 -> output-ESP32:#JTAG#1847
- U$370: device output-ESP32:#23#PICO#321866 -> output-ESP32:ESP321855
- U$371: device output-ESP32:#19#POCI#321866 -> output-ESP32:#39#A3#321862
- U$372: device output-ESP32:#18#SCK#32321869 -> output-ESP32:#36#A0#321862
- U$373: device output-ESP32:#21#SDA#32321869 -> output-ESP32:#34#A6#32321865
- U$374: device output-ESP32:#22#SCL#32321869 -> output-ESP32:#35#A7#321862
- U$375: device output-ESP32:#27#32321869 -> output-ESP32:#32#A4#32321865
- U$376: device output-ESP32:#GND#321866 -> output-ESP32:#34#A6#321862
- U$377: device output-ESP32:#3#3V#321866 -> output-ESP32:#VIN#321862
- U$378: device output-ESP32:#MEAS#1851 -> output-ESP32:#GND#321863
- U$379: device output-ESP32:#BYP#35 -> output-ESP32:#5V#321864
- U$380: device output-ESP32:D#32321863 -> output-ESP32:#3#3V#321864
- U$381: device output-ESP32:D#32321862 -> output-ESP32:#GND#321863
- U$382: device output-ESP32:G32321864 -> output-ESP32:##RESET##321864
- U$383: device output-ESP32:#1849 -> output-ESP32:#IOREF#321865
- U$384: device output-ESP32:#1850 -> output-ESP32:#13#TCK#32321869
- U$385: device output-ESP32:#I2C#1855 -> output-ESP32:#14#TMS#32321869
- U$386: device output-ESP32:##ALERT##1852 -> output-ESP32:#16#32321869
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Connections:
- removed net N$105 (its old number): D24.C, R119.2
- removed net N$32 (its old number): D8.C, R31.2
- removed net N$45 (its old number): R52.2, U11.1
- removed net N$46 (its old number): D11.C, R52.1
- removed net N$51 (its old number): D12.C, R59.2
- removed net N$59 (its old number): D14.C, R61.2
- removed net N$60 (its old number): JP37.3, R69.2
- removed net N$78 (its old number): D18.C, R89.2
- removed net N$79 (its old number): D15.C, R68.2
- removed net N$85 (its old number): D19.C, R92.2
- removed net N$87 (its old number): JP51.3, R99.2
- removed net N$88 (its old number): JP51.1, R100.2
- removed net VBUS: BYP.1, C4.1, F1.1, J2.VBUS1, J2.VBUS2, J3.VBUS
- removed net VBUS1: BYP1.1, C18.1, F2.1, J21.VBUS1, J21.VBUS2, J22.VBUS
- removed net VBUS2: BYP2.1, C35.1, F3.1, J37.VBUS1, J37.VBUS2, J38.VBUS
- removed net VBUS3: BYP3.1, C52.1, F4.1, J53.VBUS1, J53.VBUS2, J54.VBUS
- new net N$101: JP60.2, R89.1
- new net N$102: JP63.2, R68.1
- new net N$107: D23.C, R91.2
- new net N$108: JP72.3, R99.2
- new net N$109: JP72.1, R100.2
- new net N$120: JP80.2, U23.1
- new net N$125: D27.C, R119.2
- new net N$126: D24.C, R98.2
- new net N$129: BYP3.1, C52.1, F4.1, JP77.2, JP77.4
- new net N$130: J58.9, JP79.1
- new net N$131: JP83.2, R92.1
- new net N$132: JP82.2, R91.1
- new net N$133: JP80.1, R112.2
- new net N$134: D26.C, R112.1
- new net N$135: JP81.2, R119.1
- new net N$136: JP84.2, R98.1
- new net N$19: BYP.1, C4.1, F1.1, JP10.2, JP10.4
- new net N$27: J15.9, JP16.1
- new net N$30: JP20.2, R4.1
- new net N$38: D8.C, R32.2
- new net N$39: D9.C, R31.2
- new net N$4: JP17.1, R21.2
- new net N$40: JP30.3, R39.2
- new net N$41: JP30.1, R40.2
- new net N$57: D13.C, R59.2
- new net N$62: J28.9, JP37.1
- new net N$63: JP41.2, R32.1
- new net N$64: JP40.2, R31.1
- new net N$65: JP38.1, R52.2
- new net N$66: D12.C, R52.1
- new net N$67: JP39.2, R59.1
- new net N$68: JP42.2, R38.1
- new net N$74: JP51.3, R69.2
- new net N$75: JP51.1, R70.2
- new net N$91: D20.C, R89.2
- new net N$92: D17.C, R68.2
- new net N$95: BYP2.1, C35.1, F3.1, JP56.2, JP56.4
- new net N$96: J43.9, JP58.1
- new net N$97: JP62.2, R62.1
- new net N$98: JP61.2, R61.1
- new net SHLD: J2.SHLD1, J2.SHLD2, J2.SHLD3, J2.SHLD4, J2.SHLD5, J2.SHLD6, J2.SHLD7, J2.SHLD8, JP15.2
- new net SHLD1: J20.SHLD1, J20.SHLD2, J20.SHLD3, J20.SHLD4, J20.SHLD5, J20.SHLD6, J20.SHLD7, J20.SHLD8, JP36.2
- new net SHLD2: J35.SHLD1, J35.SHLD2, J35.SHLD3, J35.SHLD4, J35.SHLD5, J35.SHLD6, J35.SHLD7, J35.SHLD8, JP57.2
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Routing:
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- added copper zone on layer 1, net SHLD
- added copper zone on layer 1, net SHLD1
- added copper zone on layer 1, net SHLD2
- added copper zone on layer 1, net SHLD3
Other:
- board size 172.2 x 137.9 mm -> 175.3 x 131.1 mm
- board text added: "v02"
- board text removed: "v01"
